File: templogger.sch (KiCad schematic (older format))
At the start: 20 parts, among them J1 USB_A, J2 Conn_01x03, U1 MCP2221, U2 ATtiny3216-S, U3 LM35-LP, U4 SC39_11_RT, U5 SC39_11_RT, U6 SC_39_11_RT, U7 SC_39_11_RT

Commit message: First PCB Layout
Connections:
- net ADC: now also U2.10 (PB1); no longer U2.3 (PA5)
- net Seg_2: now also U2.6 (PB5); no longer U2.4 (PA6)
- net Seg_DP: now also U2.7 (PB4); no longer U2.5 (PA7)
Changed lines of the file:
@@
 Wire Wire Line
 	6100 5100 6500 5100
-Wire Wire Line
-	6100 5200 6500 5200
-Wire Wire Line
-	6100 5300 6500 5300
-Text GLabel 6500 5300 2    50   Input ~ 0
+Text GLabel 6100 5900 2    50   Input ~ 0
 Seg_DP
-Text GLabel 6500 5200 2    50   Input ~ 0
+Text GLabel 6100 6000 2    50   Input ~ 0
 Seg_2
-Text GLabel 6500 5100 2    50   Input ~ 0
+Text GLabel 6100 5600 2    50   Input ~ 0
 ADC
 Text GLabel 6500 5000 2    50   Input ~ 0
@@
 Seg_F
 $Comp
-L power:GND #PWR?
+L power:GND #PWR0118
 U 1 1 5EC8A53C
 P 4500 3100
-F 0 "#PWR?" H 4500 2850 50  0001 C CNN
+F 0 "#PWR0118" H 4500 2850 50  0001 C CNN
 F 1 "GND" H 4505 2927 50  0000 C CNN
 F 2 "" H 4500 3100 50  0001 C CNN

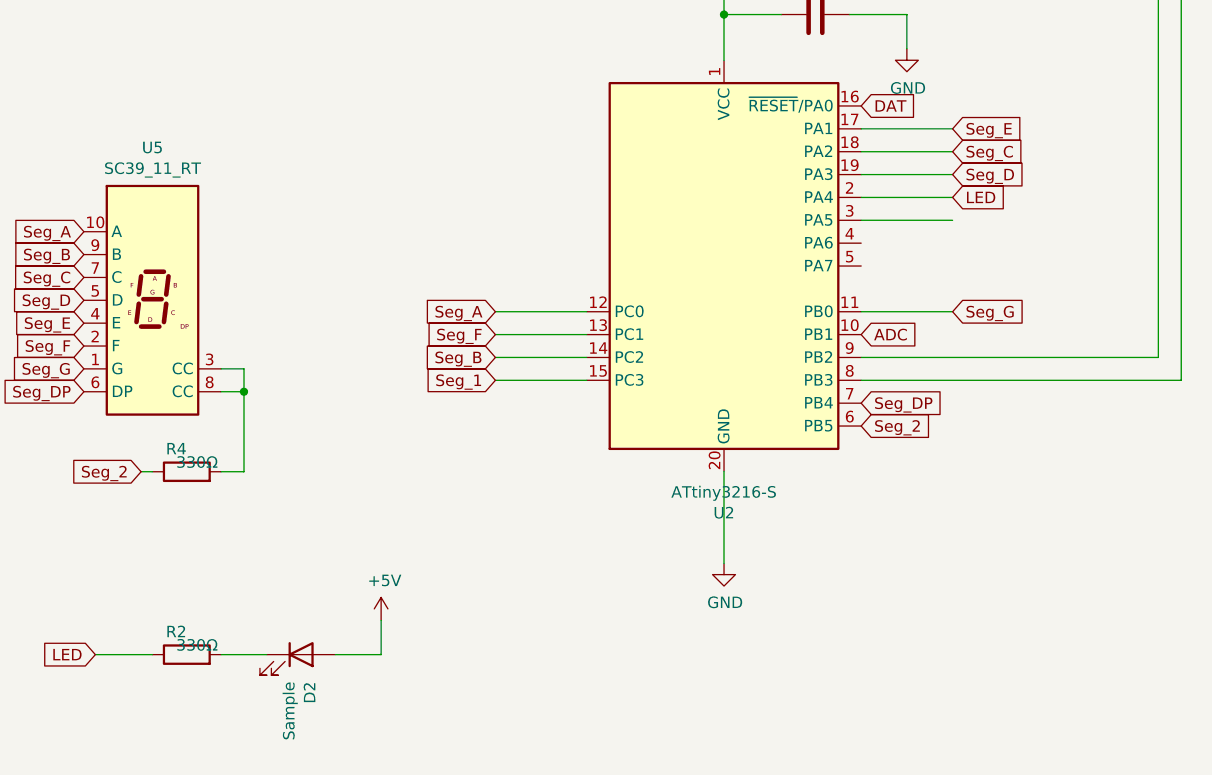
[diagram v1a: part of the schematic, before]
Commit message: Optimize routing. not done...
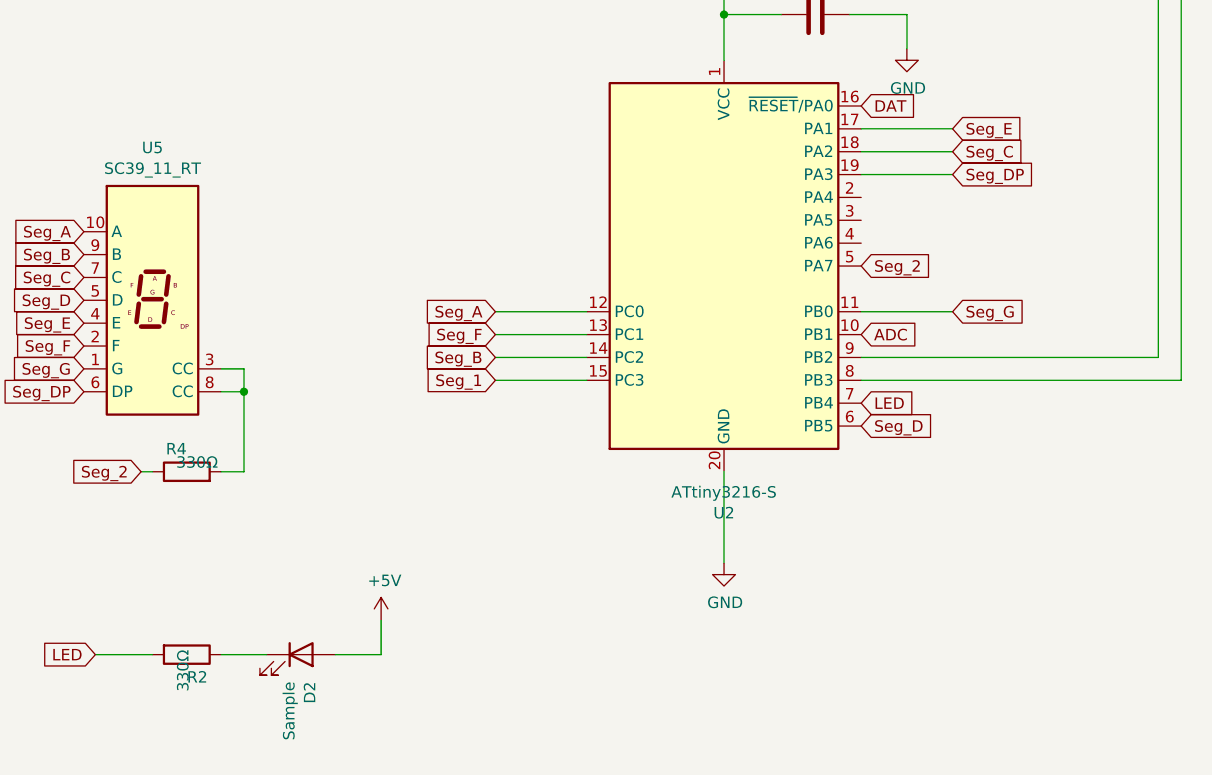
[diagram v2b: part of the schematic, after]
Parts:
- removed U6, U7: SC_39_11_RT, symbol sc_39_11_rt:SC_39_11_RT
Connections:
- net LED: now also R2.2, U2.7 (PB4); no longer R2.1, U2.2 (PA4)
- net Seg_2: now also U2.5 (PA7); no longer U2.6 (PB5)
- net Seg_D: now also U2.6 (PB5); no longer U2.19 (PA3)
- net Seg_DP: now also U2.19 (PA3); no longer U2.7 (PB4)
- net at D2.1 (K): now also R2.1; no longer R2.2
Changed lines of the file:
@@
 Wire Wire Line
 	6100 4900 6500 4900
-Wire Wire Line
-	6100 5000 6500 5000
-Wire Wire Line
-	6100 5100 6500 5100
-Text GLabel 6100 5900 2    50   Input ~ 0
+Text GLabel 6500 4900 2    50   Input ~ 0
 Seg_DP
-Text GLabel 6100 6000 2    50   Input ~ 0
+Text GLabel 6100 5300 2    50   Input ~ 0
 Seg_2
 Text GLabel 6100 5600 2    50   Input ~ 0
 ADC
-Text GLabel 6500 5000 2    50   Input ~ 0
-LED
-Text GLabel 6500 4900 2    50   Input ~ 0
-Seg_D
 Text GLabel 6500 4800 2    50   Input ~ 0
 Seg_C
@@
 Text GLabel 10100 1900 2    50   Input ~ 0
 ADC
-$Comp
-L sc_39_11_rt:SC_39_11_RT U6
-U 1 1 5EC43A7E
-P 1950 5250
-F 0 "U6" H 1975 5250 50  0001 L CNN
-F 1 "SC_39_11_RT" H 1975 5205 50  0001 L CNN
-F 2 "" H 1950 5250 50  0001 C CNN
-F 3 "" H 1950 5250 50  0001 C CNN
-	1    1950 5250
-	1    0    0    -1
-$EndComp
-$Comp
-L sc_39_11_rt:SC39_11_RT U4
-U 1 1 5EC46DC7
-P 1600 5450
-F 0 "U4" H 1600 6117 50  0000 C CNN
-F 1 "SC39_11_RT" H 1600 6026 50  0000 C CNN
-F 2 "My Footprints:SC39-11_RT_small" H 1600 4900 50  0001 C CNN
-F 3 "http://www.kingbrightusa.com/images/catalog/SPEC/sc39-11ewa.pdf" H 1600 5450 50  0001 C CNN
-	1    1600 5450
-	1    0    0    -1
-$EndComp
 Text GLabel 1300 5550 0    50   Input ~ 0
 Seg_E
@@
 Wire Wire Line
 	1600 6200 1550 6200
-$Comp
-L sc_39_11_rt:SC_39_11_RT U7
-U 1 1 5EC9870E
-P 3350 5250
-F 0 "U7" H 3375 5250 50  0001 L CNN
-F 1 "SC_39_11_RT" H 3375 5205 50  0001 L CNN
-F 2 "" H 3350 5250 50  0001 C CNN
-F 3 "" H 3350 5250 50  0001 C CNN
-	1    3350 5250
-	1    0    0    -1
-$EndComp
-$Comp
-L sc_39_11_rt:SC39_11_RT U5
-U 1 1 5EC98714
-P 3000 5450
-F 0 "U5" H 3000 6117 50  0000 C CNN
-F 1 "SC39_11_RT" H 3000 6026 50  0000 C CNN
-F 2 "My Footprints:SC39-11_RT_small" H 3000 4900 50  0001 C CNN
-F 3 "http://www.kingbrightusa.com/images/catalog/SPEC/sc39-11ewa.pdf" H 3000 5450 50  0001 C CNN
-	1    3000 5450
-	1    0    0    -1
-$EndComp
 Text GLabel 2700 5550 0    50   Input ~ 0
 Seg_E
@@
 	2750 7000 3000 7000
 $Comp
-L Device:R R2
-U 1 1 5ECB072C
-P 3150 7000
-F 0 "R2" V 3220 7046 50  0000 C TNN
-F 1 "330Ω" V 3220 6955 50  0000 C BNN
-F 2 "Resistor_THT:R_Axial_DIN0207_L6.3mm_D2.5mm_P2.54mm_Vertical" V 3080 7000 50  0001 C CNN
-F 3 "~" H 3150 7000 50  0001 C CNN
-	1    3150 7000
-	0    -1   -1   0
-$EndComp
-$Comp
 L Device:LED D2
 U 1 1 5ECB1CCD
@@
 	1    0    0    -1
 $EndComp
+$Comp
+L sc_39_11_rt:SC39_11_RT U5
+U 1 1 5EC98714
+P 3000 5450
+F 0 "U5" H 3000 6117 50  0000 C CNN
+F 1 "SC39_11_RT" H 3000 6026 50  0000 C CNN
+F 2 "My Footprints:SC39-11_RT_small" H 3000 4900 50  0001 C CNN
+F 3 "http://www.kingbrightusa.com/images/catalog/SPEC/sc39-11ewa.pdf" H 3000 5450 50  0001 C CNN
+	1    3000 5450
+	1    0    0    -1
+$EndComp
+$Comp
+L sc_39_11_rt:SC39_11_RT U4
+U 1 1 5EC46DC7
+P 1600 5450
+F 0 "U4" H 1600 6117 50  0000 C CNN
+F 1 "SC39_11_RT" H 1600 6026 50  0000 C CNN
+F 2 "My Footprints:SC39-11_RT_small" H 1600 4900 50  0001 C CNN
+F 3 "http://www.kingbrightusa.com/images/catalog/SPEC/sc39-11ewa.pdf" H 1600 5450 50  0001 C CNN
+	1    1600 5450
+	1    0    0    -1
+$EndComp
+$Comp
+L Device:R R2
+U 1 1 5ECB072C
+P 3150 7000
+F 0 "R2" V 3220 7046 50  0000 C TNN
+F 1 "330Ω" H 3220 6955 50  0000 C BNN
+F 2 "Resistor_THT:R_Axial_DIN0207_L6.3mm_D2.5mm_P2.54mm_Vertical" V 3080 7000 50  0001 C CNN
+F 3 "~" H 3150 7000 50  0001 C CNN
+	1    3150 7000
+	0    1    1    0
+$EndComp
+Text GLabel 6100 5900 2    50   Input ~ 0
+LED
+Text GLabel 6100 6000 2    50   Input ~ 0
+Seg_D
 $EndSCHEMATC
